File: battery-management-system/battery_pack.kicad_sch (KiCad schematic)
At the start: 16 parts, among them J1 CELL4_PLUS, J2 CELL4_MINUS, J3 CELL3_MINUS, J4 CELL2_MINUS, J5 CELL1_MINUS, J6 VBAT+, J8 VBAT-, Q1 DMN3730U, Q2 TJ40S04M3L, Q3 TJ40S04M3L, Q4 DMN3730U

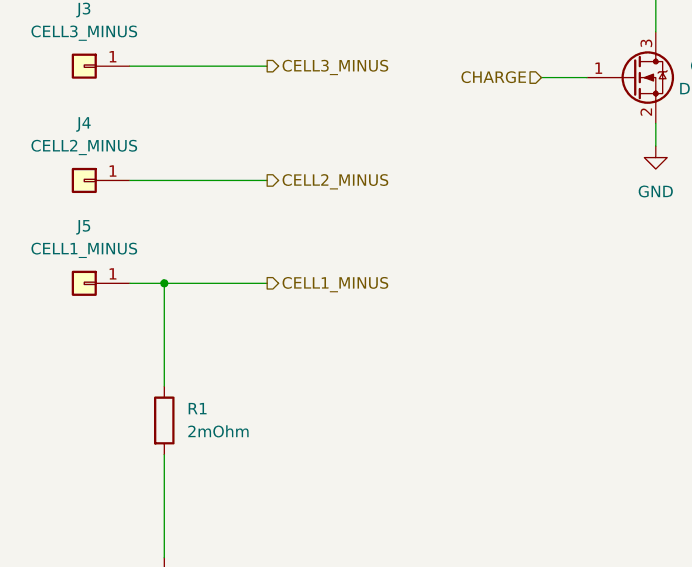
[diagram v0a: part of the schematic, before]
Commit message: implement cell measurement
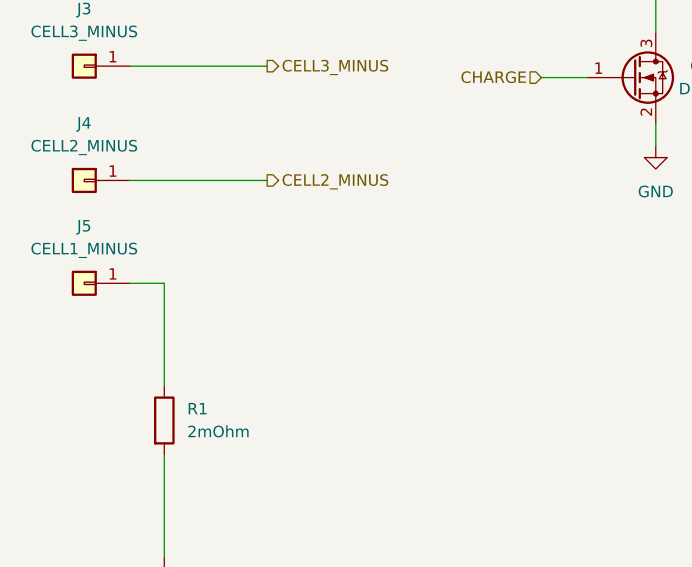
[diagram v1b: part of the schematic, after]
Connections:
- net CELL1_MINUS: no longer names the net of J5.1 (Pin_1), R1.1
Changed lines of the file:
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@@
   (junction (at 187.96 45.72) (diameter 0) (color 0 0 0 0)
-  )
-  (junction (at 74.93 114.3) (diameter 0) (color 0 0 0 0)
   )
   (junction (at 119.38 60.96) (diameter 0) (color 0 0 0 0)
@@
   )
   (wire (pts (xy 119.38 60.96) (xy 119.38 63.5))
-    (stroke (width 0) (type default) (color 0 0 0 0))
-  )
-  (wire (pts (xy 74.93 114.3) (xy 86.36 114.3))
     (stroke (width 0) (type default) (color 0 0 0 0))
   )
@@
     (effects (font (size 1.27 1.27)) (justify right))
   )
-  (hierarchical_label "CELL1_MINUS" (shape output) (at 86.36 114.3 0)
-    (effects (font (size 1.27 1.27)) (justify left))
-  )
   (hierarchical_label "CELL3_MINUS" (shape output) (at 86.36 90.17 0)

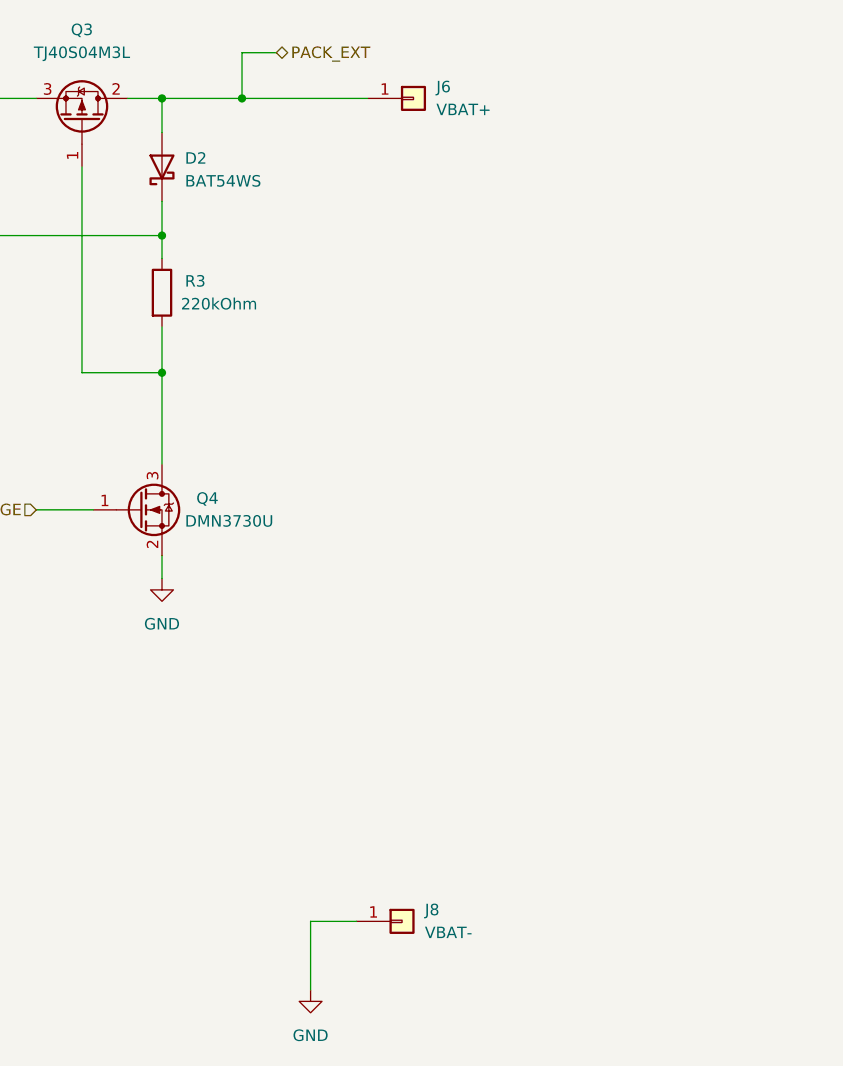
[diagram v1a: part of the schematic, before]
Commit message: route UART and ADC channels on MCU
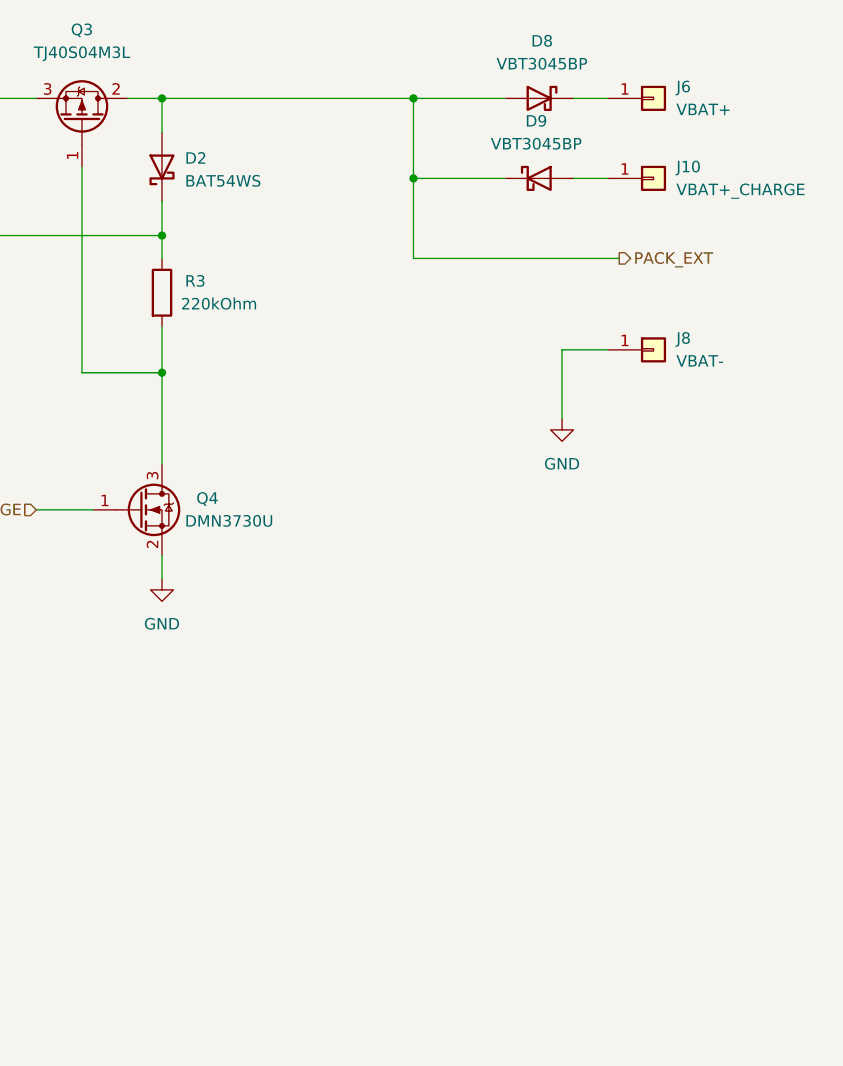
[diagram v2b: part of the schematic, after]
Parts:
- added D8, D9: VBT3045BP, benediktibk:D_SOD-323, symbol benediktibk:VBT3045BP
- added J10: VBAT+_CHARGE, benediktibk:Connector_M6, symbol benediktibk:Connector_M6
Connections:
- net PACK_EXT: now also D8.2 (K), D9.2 (K); no longer J6.1 (Pin_1)
- new net: D8.2 (K), J6.1 (Pin_1)
- new net: D9.2 (K), J10.1 (Pin_1)
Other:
- moved on the sheet: J6, J8
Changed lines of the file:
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@@
 (kicad_sch (version 20211123) (generator eeschema)
   (paper "A4")
-  (junction (at 187.96 45.72) (diameter 0) (color 0 0 0 0)
+  (junction (at 207.01 54.61) (diameter 0) (color 0 0 0 0)
   )
   (junction (at 119.38 60.96) (diameter 0) (color 0 0 0 0)
   )
+  (junction (at 207.01 45.72) (diameter 0) (color 0 0 0 0)
+  )
   (junction (at 179.07 60.96) (diameter 0) (color 0 0 0 0)
   )
@@
     (stroke (width 0) (type default) (color 0 0 0 0))
   )
+  (wire (pts (xy 217.17 54.61) (xy 207.01 54.61))
+    (stroke (width 0) (type default) (color 0 0 0 0))
+  )
   (wire (pts (xy 119.38 60.96) (xy 119.38 63.5))
     (stroke (width 0) (type default) (color 0 0 0 0))
@@
     (stroke (width 0) (type default) (color 0 0 0 0))
   )
+  (wire (pts (xy 224.79 54.61) (xy 228.6 54.61))
+    (stroke (width 0) (type default) (color 0 0 0 0))
+  )
   (wire (pts (xy 71.12 78.74) (xy 86.36 78.74))
     (stroke (width 0) (type default) (color 0 0 0 0))
   )
-  (wire (pts (xy 195.58 137.16) (xy 200.66 137.16))
+  (wire (pts (xy 223.52 73.66) (xy 228.6 73.66))
     (stroke (width 0) (type default) (color 0 0 0 0))
   )
@@
     (stroke (width 0) (type default) (color 0 0 0 0))
   )
-  (wire (pts (xy 191.77 40.64) (xy 187.96 40.64))
-    (stroke (width 0) (type default) (color 0 0 0 0))
-  )
   (wire (pts (xy 179.07 96.52) (xy 179.07 99.06))
     (stroke (width 0) (type default) (color 0 0 0 0))
@@
     (stroke (width 0) (type default) (color 0 0 0 0))
   )
-  (wire (pts (xy 187.96 45.72) (xy 201.93 45.72))
+  (wire (pts (xy 224.79 45.72) (xy 228.6 45.72))
     (stroke (width 0) (type default) (color 0 0 0 0))
   )
@@
     (stroke (width 0) (type default) (color 0 0 0 0))
   )
+  (wire (pts (xy 229.87 63.5) (xy 207.01 63.5))
+    (stroke (width 0) (type default) (color 0 0 0 0))
+  )
   (wire (pts (xy 119.38 57.15) (xy 119.38 60.96))
     (stroke (width 0) (type default) (color 0 0 0 0))
@@
     (stroke (width 0) (type default) (color 0 0 0 0))
   )
-  (wire (pts (xy 187.96 40.64) (xy 187.96 45.72))
-    (stroke (width 0) (type default) (color 0 0 0 0))
-  )
   (wire (pts (xy 74.93 114.3) (xy 74.93 125.73))
     (stroke (width 0) (type default) (color 0 0 0 0))
   )
-  (wire (pts (xy 195.58 144.78) (xy 195.58 137.16))
+  (wire (pts (xy 207.01 45.72) (xy 217.17 45.72))
+    (stroke (width 0) (type default) (color 0 0 0 0))
+  )
+  (wire (pts (xy 223.52 81.28) (xy 223.52 73.66))
     (stroke (width 0) (type default) (color 0 0 0 0))
   )
@@
     (stroke (width 0) (type default) (color 0 0 0 0))
   )
+  (wire (pts (xy 207.01 54.61) (xy 207.01 45.72))
+    (stroke (width 0) (type default) (color 0 0 0 0))
+  )
   (wire (pts (xy 124.46 45.72) (xy 119.38 45.72))
     (stroke (width 0) (type default) (color 0 0 0 0))
@@
     (stroke (width 0) (type default) (color 0 0 0 0))
   )
-  (wire (pts (xy 179.07 45.72) (xy 187.96 45.72))
+  (wire (pts (xy 179.07 45.72) (xy 207.01 45.72))
     (stroke (width 0) (type default) (color 0 0 0 0))
   )
@@
   )
   (wire (pts (xy 170.18 76.2) (xy 170.18 53.34))
+    (stroke (width 0) (type default) (color 0 0 0 0))
+  )
+  (wire (pts (xy 207.01 63.5) (xy 207.01 54.61))
     (stroke (width 0) (type default) (color 0 0 0 0))
   )
@@
     (effects (font (size 1.27 1.27)) (justify left))
   )
-  (hierarchical_label "PACK_EXT" (shape bidirectional) (at 191.77 40.64 0)
+  (hierarchical_label "PACK_EXT" (shape output) (at 229.87 63.5 0)
     (effects (font (size 1.27 1.27)) (justify left))
   )
@@
     (pin "2")
   )
-  (symbol (lib_id "benediktibk:Connector_M6") (at 205.74 137.16 0) (unit 1)
-    (in_bom yes) (on_board yes) (fields_autoplaced)
-    (property "Reference" "J8" (id 0) (at 208.28 135.8899 0)
-      (effects (font (size 1.27 1.27)) (justify left))
-    )
-    (property "Value" "VBAT-" (id 1) (at 208.28 138.4299 0)
-      (effects (font (size 1.27 1.27)) (justify left))
-    )
-    (property "Footprint" "benediktibk:Connector_M6" (id 2) (at 205.994 133.096 0)
-      (effects (font (size 1.27 1.27)) hide)
-    )
-    (property "Datasheet" "~" (id 3) (at 205.74 137.16 0)
-      (effects (font (size 1.27 1.27)) hide)
-    )
-    (property "RS order number" "" (id 4) (at 205.74 137.16 0)
-      (effects (font (size 1.27 1.27)) hide)
-    )
-    (pin "1")
-  )
-  (symbol (lib_id "benediktibk:Connector_M6") (at 207.01 45.72 0) (unit 1)
-    (in_bom yes) (on_board yes) (fields_autoplaced)
-    (property "Reference" "J6" (id 0) (at 209.55 44.4499 0)
-      (effects (font (size 1.27 1.27)) (justify left))
-    )
-    (property "Value" "VBAT+" (id 1) (at 209.55 46.9899 0)
-      (effects (font (size 1.27 1.27)) (justify left))
-    )
-    (property "Footprint" "benediktibk:Connector_M6" (id 2) (at 207.264 41.656 0)
-      (effects (font (size 1.27 1.27)) hide)
-    )
-    (property "Datasheet" "~" (id 3) (at 207.01 45.72 0)
-      (effects (font (size 1.27 1.27)) hide)
-    )
-    (property "RS order number" "" (id 4) (at 207.01 45.72 0)
-      (effects (font (size 1.27 1.27)) hide)
-    )
-    (pin "1")
+  (symbol (lib_id "benediktibk:Connector_M6") (at 233.68 73.66 0) (unit 1)
+    (in_bom yes) (on_board yes) (fields_autoplaced)
+    (property "Reference" "J8" (id 0) (at 236.22 72.3899 0)
+      (effects (font (size 1.27 1.27)) (justify left))
+    )
+    (property "Value" "VBAT-" (id 1) (at 236.22 74.9299 0)
+      (effects (font (size 1.27 1.27)) (justify left))
+    )
+    (property "Footprint" "benediktibk:Connector_M6" (id 2) (at 233.934 69.596 0)
+      (effects (font (size 1.27 1.27)) hide)
+    )
+    (property "Datasheet" "~" (id 3) (at 233.68 73.66 0)
+      (effects (font (size 1.27 1.27)) hide)
+    )
+    (property "RS order number" "" (id 4) (at 233.68 73.66 0)
+      (effects (font (size 1.27 1.27)) hide)
+    )
+    (pin "1")
+  )
+  (symbol (lib_id "benediktibk:VBT3045BP") (at 220.98 45.72 0) (mirror y) (unit 1)
+    (in_bom yes) (on_board yes) (fields_autoplaced)
+    (property "Reference" "D8" (id 0) (at 221.2975 39.37 0))
+    (property "Value" "VBT3045BP" (id 1) (at 221.2975 41.91 0))
+    (property "Footprint" "benediktibk:D_SOD-323" (id 2) (at 220.218 42.418 0)
+      (effects (font (size 1.27 1.27)) hide)
+    )
+    (property "Datasheet" "" (id 3) (at 220.98 45.72 0)
+      (effects (font (size 0 0)) hide)
+    )
+    (property "RS order number" "768-9269" (id 4) (at 222.504 50.8 0)
+      (effects (font (size 1.27 1.27)) hide)
+    )
+    (pin "2")
+    (pin "2")
+  )
+  (symbol (lib_id "benediktibk:Connector_M6") (at 233.68 45.72 0) (unit 1)
+    (in_bom yes) (on_board yes) (fields_autoplaced)
+    (property "Reference" "J6" (id 0) (at 236.22 44.4499 0)
+      (effects (font (size 1.27 1.27)) (justify left))
+    )
+    (property "Value" "VBAT+" (id 1) (at 236.22 46.9899 0)
+      (effects (font (size 1.27 1.27)) (justify left))
+    )
+    (property "Footprint" "benediktibk:Connector_M6" (id 2) (at 233.934 41.656 0)
+      (effects (font (size 1.27 1.27)) hide)
+    )
+    (property "Datasheet" "~" (id 3) (at 233.68 45.72 0)
+      (effects (font (size 1.27 1.27)) hide)
+    )
+    (property "RS order number" "" (id 4) (at 233.68 45.72 0)
+      (effects (font (size 1.27 1.27)) hide)
+    )
+    (pin "1")
+  )
+  (symbol (lib_id "benediktibk:VBT3045BP") (at 220.98 54.61 0) (unit 1)
+    (in_bom yes) (on_board yes) (fields_autoplaced)
+    (property "Reference" "D9" (id 0) (at 220.6625 48.26 0))
+    (property "Value" "VBT3045BP" (id 1) (at 220.6625 50.8 0))
+    (property "Footprint" "benediktibk:D_SOD-323" (id 2) (at 221.742 51.308 0)
+      (effects (font (size 1.27 1.27)) hide)
+    )
+    (property "Datasheet" "" (id 3) (at 220.98 54.61 0)
+      (effects (font (size 0 0)) hide)
+    )
+    (property "RS order number" "768-9269" (id 4) (at 219.456 59.69 0)
+      (effects (font (size 1.27 1.27)) hide)
+    )
+    (pin "2")
+    (pin "2")
   )
   (symbol (lib_id "benediktibk:Connector_M6") (at 66.04 90.17 0) (mirror y) (unit 1)
@@
     (pin "2")
   )
+  (symbol (lib_id "benediktibk:Connector_M6") (at 233.68 54.61 0) (unit 1)
+    (in_bom yes) (on_board yes) (fields_autoplaced)
+    (property "Reference" "J10" (id 0) (at 236.22 53.3399 0)
+      (effects (font (size 1.27 1.27)) (justify left))
+    )
+    (property "Value" "VBAT+_CHARGE" (id 1) (at 236.22 55.8799 0)
+      (effects (font (size 1.27 1.27)) (justify left))
+    )
+    (property "Footprint" "benediktibk:Connector_M6" (id 2) (at 233.934 50.546 0)
+      (effects (font (size 1.27 1.27)) hide)
+    )
+    (property "Datasheet" "~" (id 3) (at 233.68 54.61 0)
+      (effects (font (size 1.27 1.27)) hide)
+    )
+    (property "RS order number" "" (id 4) (at 233.68 54.61 0)
+      (effects (font (size 1.27 1.27)) hide)
+    )
+    (pin "1")
+  )
   (symbol (lib_id "benediktibk:Connector_M6") (at 66.04 78.74 0) (mirror y) (unit 1)
     (in_bom yes) (on_board yes) (fields_autoplaced)
@@
     (pin "1")
   )
-  (symbol (lib_id "power:GND") (at 195.58 144.78 0) (unit 1)
-    (in_bom yes) (on_board yes) (fields_autoplaced)
-    (property "Reference" "#PWR0116" (id 0) (at 195.58 151.13 0)
-      (effects (font (size 1.27 1.27)) hide)
-    )
-    (property "Value" "GND" (id 1) (at 195.58 149.86 0))
-    (property "Footprint" "" (id 2) (at 195.58 144.78 0)
-      (effects (font (size 1.27 1.27)) hide)
-    )
-    (property "Datasheet" "" (id 3) (at 195.58 144.78 0)
-      (effects (font (size 1.27 1.27)) hide)
-    )
+  (symbol (lib_id "power:GND") (at 223.52 81.28 0) (unit 1)
+    (in_bom yes) (on_board yes) (fields_autoplaced)
+    (property "Reference" "#PWR0116" (id 0) (at 223.52 87.63 0)
+      (effects (font (size 1.27 1.27)) hide)
+    )
+    (property "Value" "GND" (id 1) (at 223.52 86.36 0))
+    (property "Footprint" "" (id 2) (at 223.52 81.28 0)
+      (effects (font (size 1.27 1.27)) hide)
+    )
+    (property "Datasheet" "" (id 3) (at 223.52 81.28 0)
+      (effects (font (size 1.27 1.27)) hide)
+    )

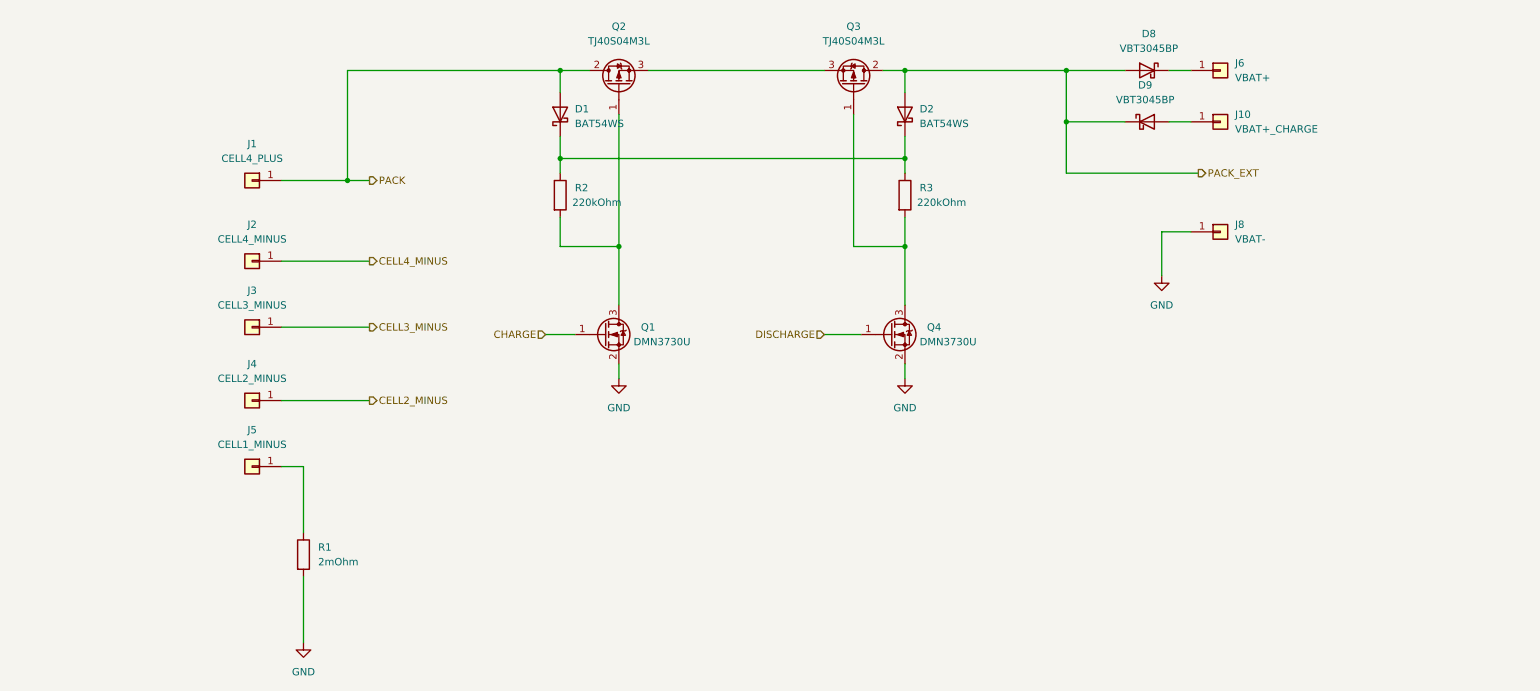
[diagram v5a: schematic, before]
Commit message: improve usage of net labels
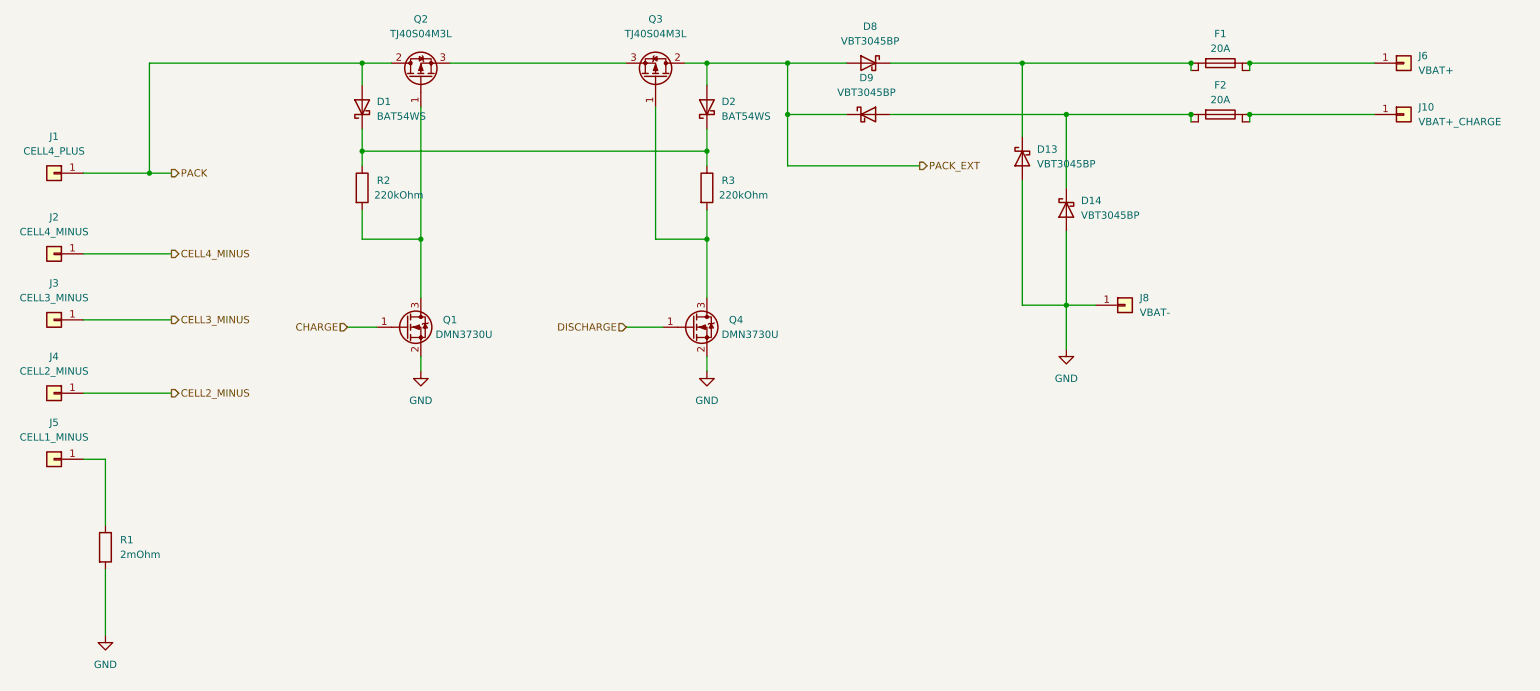
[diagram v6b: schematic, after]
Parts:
- added D13, D14: VBT3045BP, benediktibk:D_SOD-323, symbol benediktibk:VBT3045BP
- added F1, F2: 20A, benediktibk:KEYSTONE_blade_fus_holder, symbol benediktibk:KEYSTONE_blade_fuse_holder
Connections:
- net GND: now also D13.2 (K), D14.2 (K)
- net at J6.1 (Pin_1): now also F1.1, F1.2; no longer D8.2 (K)
- net at J10.1 (Pin_1): now also F2.1, F2.2; no longer D9.2 (K)
- new net: D13.2 (K), D8.2 (K), F1.3, F1.4
- new net: D14.2 (K), D9.2 (K), F2.3, F2.4
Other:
- moved on the sheet: D1, D2, D8, D9, J1, J10, J2, J3, J4, J5, J6, J8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
